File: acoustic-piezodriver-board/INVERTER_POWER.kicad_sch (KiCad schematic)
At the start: 58 parts, among them Q501 AO3400A, Q502 AO3400A, U501 NCE6005AS, U502 LM3478MM, U503 NCE6005AS, U504 LM3478MM

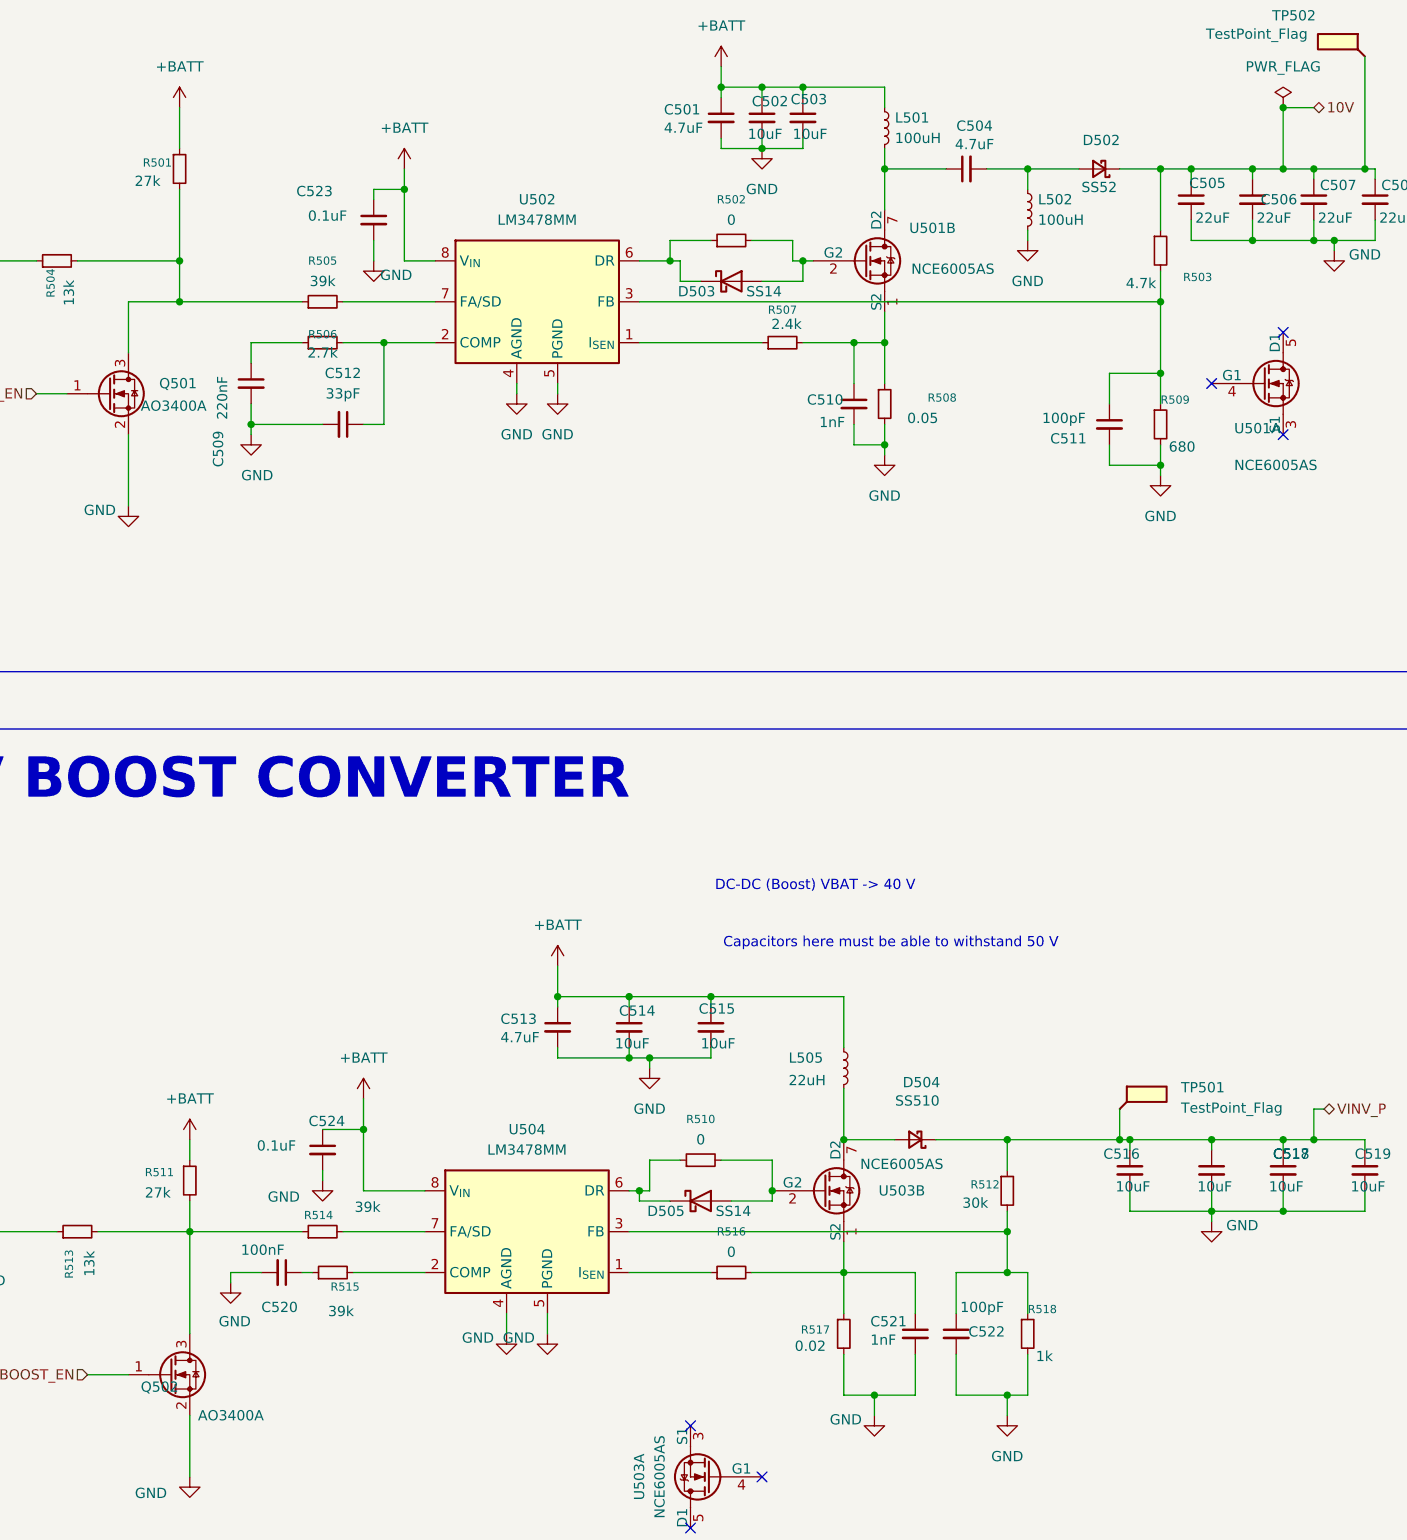
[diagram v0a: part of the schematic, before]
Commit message: Fixed ERC, DRC errors, finished routing (next) perform footprint checks
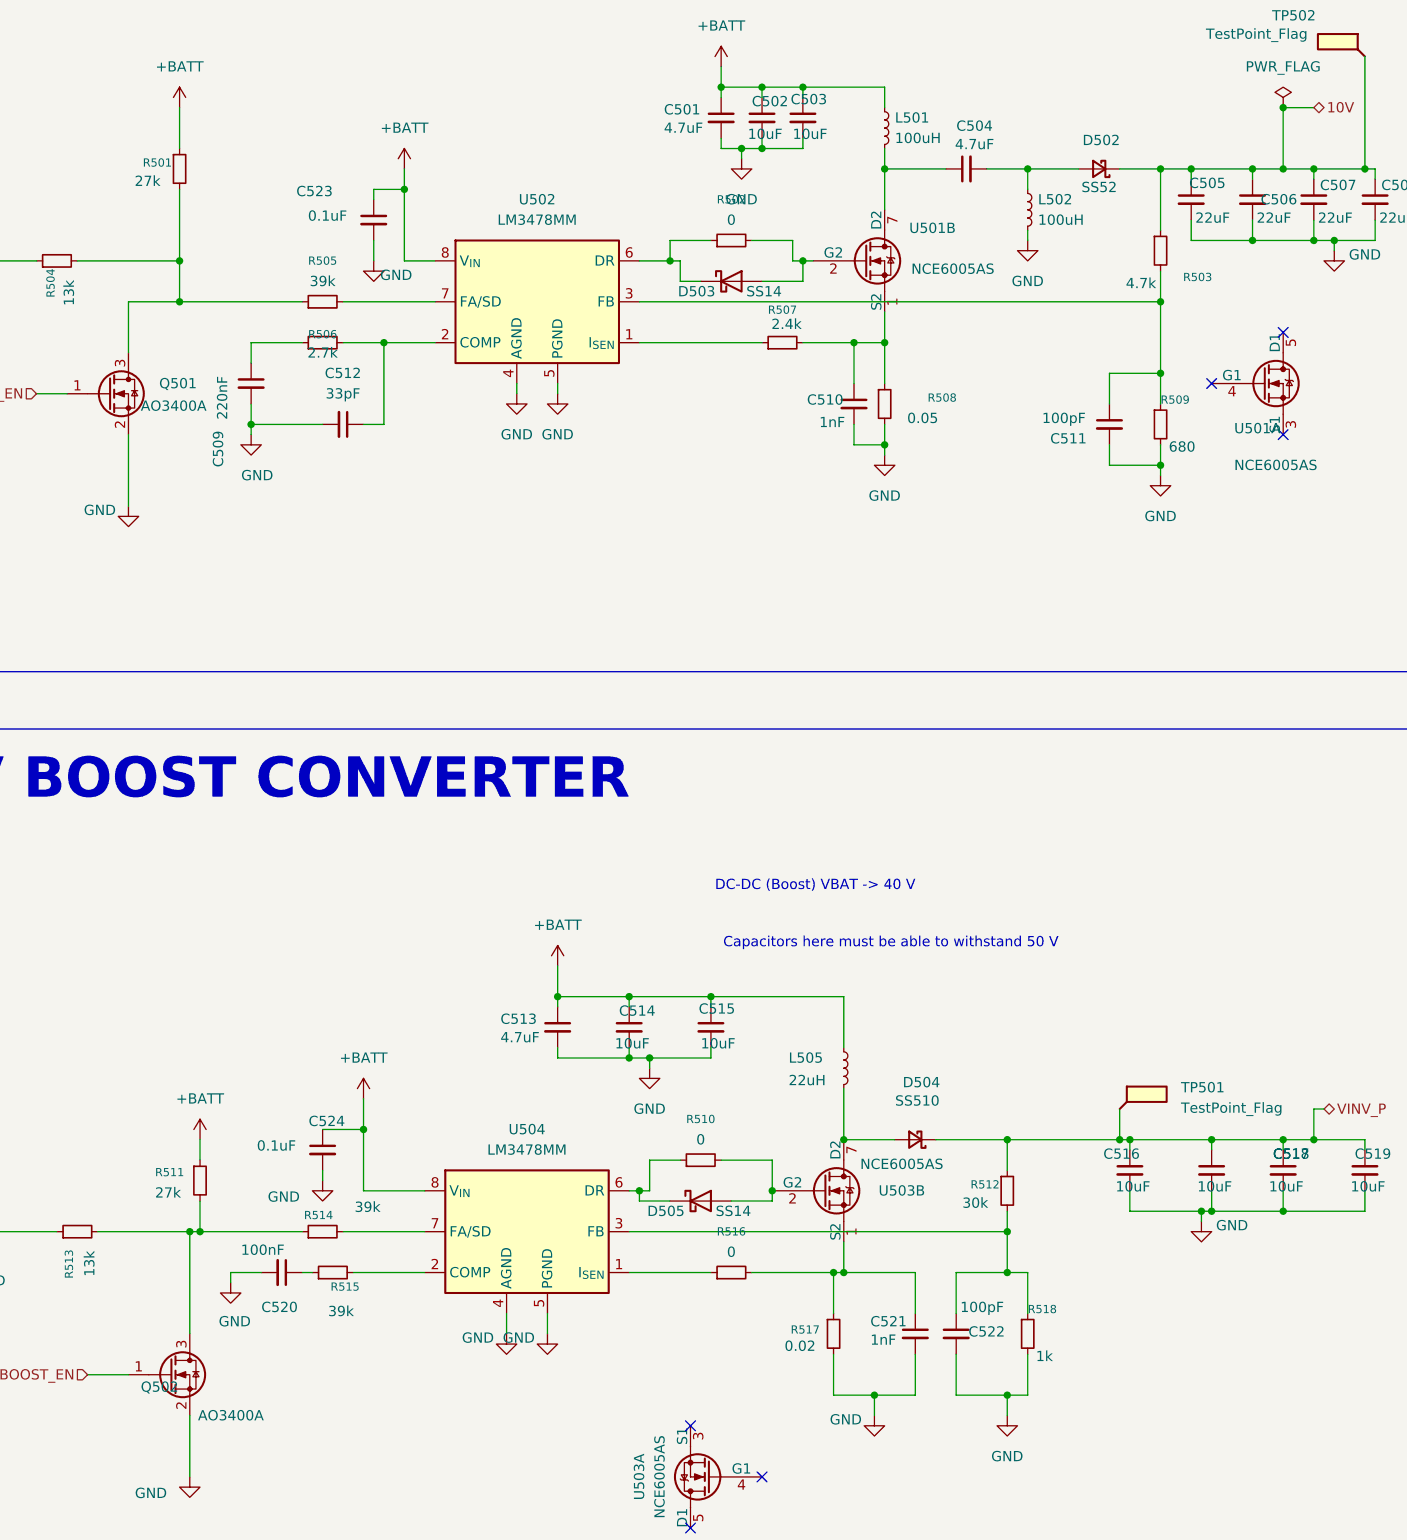
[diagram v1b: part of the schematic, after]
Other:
- moved on the sheet: R511, R517
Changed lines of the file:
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@@
 	)
 	(junction
+		(at 240.03 200.66)
+		(diameter 0)
+		(color 0 0 0 0)
+	)
+	(junction
 		(at 237.49 85.09)
 		(diameter 0)
@@
 	)
 	(junction
+		(at 307.34 66.04)
+		(diameter 0)
+		(color 0 0 0 0)
+	)
+	(junction
 		(at 293.37 171.45)
 		(diameter 0)
@@
 	)
 	(junction
+		(at 364.49 198.12)
+		(diameter 0)
+		(color 0 0 0 0)
+	)
+	(junction
 		(at 323.85 220.98)
 		(diameter 0)
@@
 	)
 	(junction
+		(at 318.77 205.74)
+		(diameter 0)
+		(color 0 0 0 0)
+	)
+	(junction
 		(at 320.04 189.23)
 		(diameter 0)
@@
 	(wire
 		(pts
+			(xy 307.34 67.31) (xy 307.34 66.04)
+		)
+		(stroke
+			(width 0)
+			(type default)
+		)
+	)
+	(wire
+		(pts
 			(xy 386.08 77.47) (xy 381 77.47)
 		)
@@
 	(wire
 		(pts
+			(xy 318.77 205.74) (xy 320.04 205.74)
+		)
+		(stroke
+			(width 0)
+			(type default)
+		)
+	)
+	(wire
+		(pts
 			(xy 295.91 191.77) (xy 295.91 195.58)
 		)
@@
 	(wire
 		(pts
-			(xy 355.6 198.12) (xy 365.76 198.12)
+			(xy 355.6 198.12) (xy 364.49 198.12)
 		)
 		(stroke
@@
 	(wire
 		(pts
-			(xy 304.8 66.04) (xy 309.88 66.04)
+			(xy 304.8 66.04) (xy 307.34 66.04)
 		)
 		(stroke
@@
 	(wire
 		(pts
+			(xy 364.49 198.12) (xy 365.76 198.12)
+		)
+		(stroke
+			(width 0)
+			(type default)
+		)
+	)
+	(wire
+		(pts
 			(xy 386.08 74.93) (xy 386.08 77.47)
 		)
@@
 	(wire
 		(pts
-			(xy 365.76 199.39) (xy 365.76 198.12)
+			(xy 364.49 199.39) (xy 364.49 198.12)
 		)
 		(stroke
@@
 	(wire
 		(pts
-			(xy 238.76 200.66) (xy 252.73 200.66)
+			(xy 238.76 200.66) (xy 240.03 200.66)
 		)
 		(stroke
@@
 	(wire
 		(pts
-			(xy 320.04 215.9) (xy 320.04 220.98)
+			(xy 318.77 215.9) (xy 318.77 220.98)
 		)
 		(stroke
@@
 	(wire
 		(pts
-			(xy 238.76 189.23) (xy 238.76 191.77)
+			(xy 240.03 189.23) (xy 240.03 191.77)
 		)
 		(stroke
@@
 	(wire
 		(pts
-			(xy 238.76 196.85) (xy 238.76 200.66)
+			(xy 240.03 196.85) (xy 240.03 200.66)
 		)
 		(stroke
@@
 	(wire
 		(pts
+			(xy 240.03 200.66) (xy 252.73 200.66)
+		)
+		(stroke
+			(width 0)
+			(type default)
+		)
+	)
+	(wire
+		(pts
 			(xy 260.35 195.58) (xy 267.97 195.58)
 		)
@@
 	(wire
 		(pts
-			(xy 323.85 220.98) (xy 320.04 220.98)
+			(xy 323.85 220.98) (xy 318.77 220.98)
 		)
 		(stroke
@@
 	(wire
 		(pts
+			(xy 307.34 66.04) (xy 309.88 66.04)
+		)
+		(stroke
+			(width 0)
+			(type default)
+		)
+	)
+	(wire
+		(pts
 			(xy 293.37 171.45) (xy 303.53 171.45)
 		)
@@
 	(wire
 		(pts
-			(xy 320.04 205.74) (xy 320.04 210.82)
+			(xy 318.77 205.74) (xy 318.77 210.82)
 		)
 		(stroke
@@
 	(wire
 		(pts
-			(xy 308.61 205.74) (xy 320.04 205.74)
+			(xy 308.61 205.74) (xy 318.77 205.74)
 		)
 		(stroke
@@
 	(symbol
 		(lib_id "Device:R_Small")
-		(at 320.04 213.36 0)
+		(at 318.77 213.36 0)
 		(unit 1)
 		(exclude_from_sim no)
@@
 		(dnp no)
 		(property "Reference" "R517"
-			(at 314.706 212.852 0)
+			(at 313.436 212.852 0)
 			(effects
 				(font
@@
 		)
 		(property "Value" "0.02"
-			(at 313.944 214.884 0)
+			(at 312.674 214.884 0)
 			(effects
 				(font
@@
 		)
 		(property "Footprint" "Resistor_SMD:R_1206_3216Metric_Pad1.30x1.75mm_HandSolder"
-			(at 320.04 213.36 0)
+			(at 318.77 213.36 0)
 			(effects
 				(font
@@
 		)
 		(property "Datasheet" "https://jlcpcb.com/api/file/downloadByFileSystemAccessId/8588919886081110016"
-			(at 320.04 213.36 0)
+			(at 318.77 213.36 0)
 			(effects
 				(font
@@
 		)
 		(property "Description" "+-1%, 333mW"
-			(at 320.04 213.36 0)
+			(at 318.77 213.36 0)
 			(effects
 				(font
@@
 		)
 		(property "MPN" "1206W3F200MT5E"
-			(at 320.04 213.36 0)
+			(at 318.77 213.36 0)
 			(effects
 				(font
@@
 		)
 		(property "LPN" "C2765435"
-			(at 320.04 213.36 0)
+			(at 318.77 213.36 0)
 			(effects
 				(font
@@
 	(symbol
 		(lib_id "Device:R_Small")
-		(at 238.76 194.31 0)
+		(at 240.03 194.31 0)
 		(unit 1)
 		(exclude_from_sim no)
@@
 		(dnp no)
 		(property "Reference" "R511"
-			(at 233.172 193.294 0)
+			(at 234.442 193.294 0)
 			(effects
 				(font
@@
 		)
 		(property "Value" "27k"
-			(at 233.172 195.834 0)
+			(at 234.442 195.834 0)
 			(effects
 				(font
@@
 		)
 		(property "Footprint" "Resistor_SMD:R_0603_1608Metric"
-			(at 238.76 194.31 0)
+			(at 240.03 194.31 0)
 			(effects
 				(font
@@
 		)
 		(property "Datasheet" "https://jlcpcb.com/api/file/downloadByFileSystemAccessId/8579706251506339840"
-			(at 238.76 194.31 0)
+			(at 240.03 194.31 0)
 			(effects
 				(font
@@
 		)
 		(property "Description" "+1%, 0.1W"
-			(at 238.76 194.31 0)
+			(at 240.03 194.31 0)
 			(effects
 				(font
@@
 		)
 		(property "LPN" "C22967"
-			(at 238.76 194.31 0)
+			(at 240.03 194.31 0)
 			(effects
 				(font
@@
 		)
 		(property "MPN" "0603WAF2702T5E"
-			(at 238.76 194.31 0)
+			(at 240.03 194.31 0)
 			(effects
 				(font
@@
 	(symbol
 		(lib_id "power:GND")
-		(at 365.76 199.39 0)
+		(at 364.49 199.39 0)
 		(unit 1)
 		(exclude_from_sim no)
@@
 		(dnp no)
 		(property "Reference" "#PWR0524"
-			(at 365.76 205.74 0)
+			(at 364.49 205.74 0)
 			(effects
 				(font
@@
 		)
 		(property "Value" "GND"
-			(at 369.57 199.898 0)
+			(at 368.3 199.898 0)
 			(effects
 				(font
@@
 		)
 		(property "Footprint" ""
-			(at 365.76 199.39 0)
+			(at 364.49 199.39 0)
 			(effects
 				(font
@@
 		)
 		(property "Datasheet" ""
-			(at 365.76 199.39 0)
+			(at 364.49 199.39 0)
 			(effects
 				(font
@@
 		)
 		(property "Description" "Power symbol creates a global label with name \"GND\" , ground"
-			(at 365.76 199.39 0)
+			(at 364.49 199.39 0)
 			(effects
 				(font
@@
 	(symbol
 		(lib_id "power:+BATT")
-		(at 238.76 189.23 0)
+		(at 240.03 189.23 0)
 		(unit 1)
 		(exclude_from_sim no)
@@
 		(fields_autoplaced yes)
 		(property "Reference" "#PWR0522"
-			(at 238.76 193.04 0)
+			(at 240.03 193.04 0)
 			(effects
 				(font
@@
 		)
 		(property "Value" "+BATT"
-			(at 238.76 184.15 0)
+			(at 240.03 184.15 0)
 			(effects
 				(font
@@
 		)
 		(property "Footprint" ""
-			(at 238.76 189.23 0)
+			(at 240.03 189.23 0)
 			(effects
 				(font
@@
 		)
 		(property "Datasheet" ""
-			(at 238.76 189.23 0)
+			(at 240.03 189.23 0)
 			(effects
 				(font
@@
 		)
 		(property "Description" "Power symbol creates a global label with name \"+BATT\""
-			(at 238.76 189.23 0)
+			(at 240.03 189.23 0)
 			(effects
 				(font
@@
 	(symbol
 		(lib_id "power:GND")
-		(at 309.88 66.04 0)
+		(at 307.34 67.31 0)
 		(unit 1)
 		(exclude_from_sim no)
@@
 		(fields_autoplaced yes)
 		(property "Reference" "#PWR0506"
-			(at 309.88 72.39 0)
+			(at 307.34 73.66 0)
 			(effects
 				(font
@@
 		)
 		(property "Value" "GND"
-			(at 309.88 71.12 0)
+			(at 307.34 72.39 0)
 			(effects
 				(font
@@
 		)
 		(property "Footprint" ""
-			(at 309.88 66.04 0)
+			(at 307.34 67.31 0)
 			(effects
 				(font
@@
 		)
 		(property "Datasheet" ""
-			(at 309.88 66.04 0)
+			(at 307.34 67.31 0)
 			(effects
 				(font
@@
 		)
 		(property "Description" "Power symbol creates a global label with name \"GND\" , ground"
-			(at 309.88 66.04 0)
+			(at 307.34 67.31 0)
 			(effects
 				(font
